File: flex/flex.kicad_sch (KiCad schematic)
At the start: 2 parts, among them J1 Conn_01x18_Pin

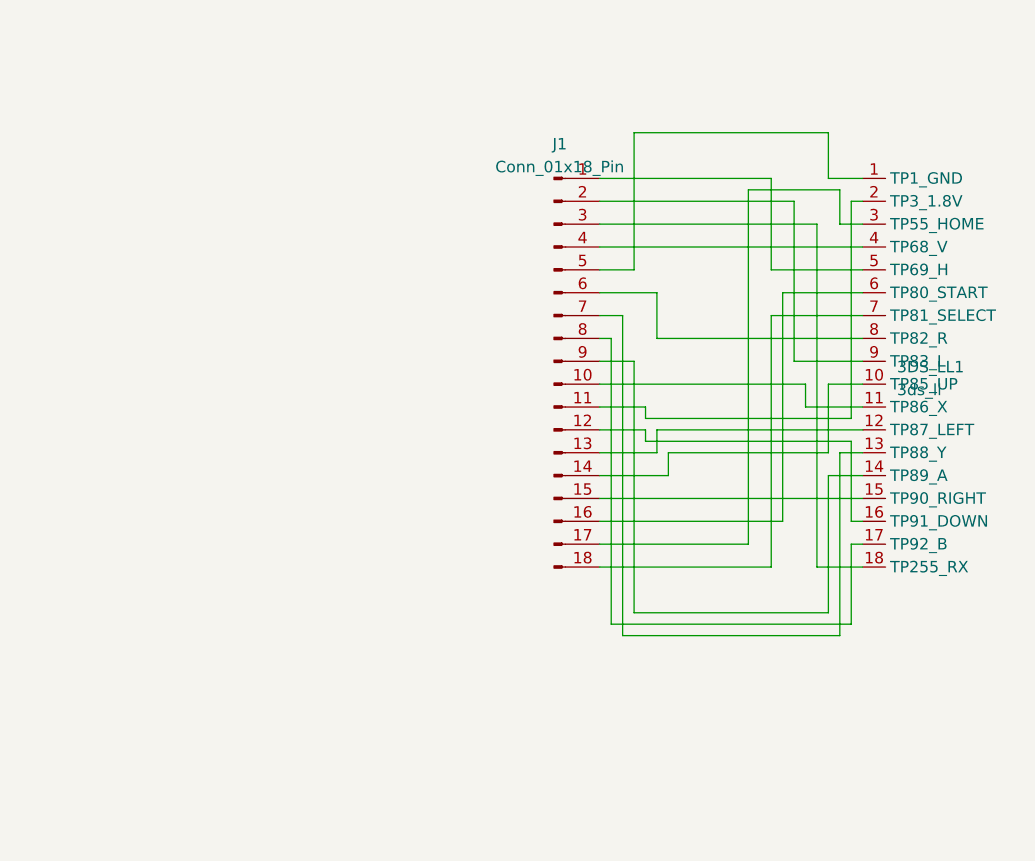
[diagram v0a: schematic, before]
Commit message: Extend flex to touch screen
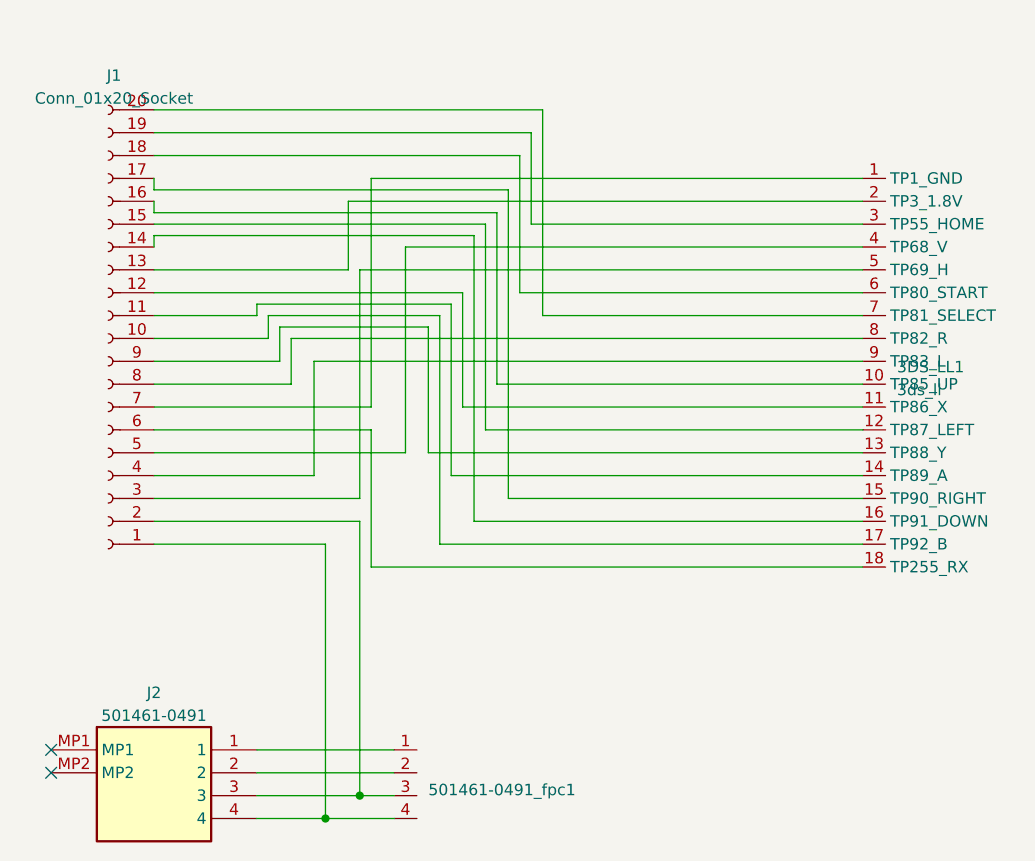
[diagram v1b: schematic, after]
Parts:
- removed J1: Conn_01x18_Pin, Connector_PinHeader_2.54mm:PinHeader_1x18_P2.54mm_Vertical, symbol Connector:Conn_01x18_Pin
- added 501461-0491_fpc1: ~, 501461-0491_fpc:501461-0491_fpc, symbol 501461-0491_fpc:501461-0491_fpc
- added J1: Conn_01x20_Socket, Connector_PinHeader_2.54mm:PinHeader_1x20_P2.54mm_Vertical, symbol Connector:Conn_01x20_Socket
- added J2: 501461-0491, 501461-0491:5014610491, symbol 501461-0491:501461-0491
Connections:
- net at 3DS_LL1.5 (TP69_H): now also J1.3 (Pin_3)
- net at 3DS_LL1.11 (TP86_X): now also J1.12 (Pin_12)
- net at 3DS_LL1.2 (TP3_1.8V): now also J1.13 (Pin_13)
- net at 3DS_LL1.16 (TP91_DOWN): now also J1.14 (Pin_14)
- net at 3DS_LL1.12 (TP87_LEFT): now also J1.15 (Pin_15)
- net at 3DS_LL1.10 (TP85_UP): now also J1.16 (Pin_16)
- net at 3DS_LL1.15 (TP90_RIGHT): now also J1.17 (Pin_17)
- net at 3DS_LL1.6 (TP80_START): now also J1.18 (Pin_18)
- net at 3DS_LL1.3 (TP55_HOME): now also J1.19 (Pin_19)
- net at 3DS_LL1.7 (TP81_SELECT): now also J1.20 (Pin_20)
- net at 3DS_LL1.9 (TP83_L): now also J1.4 (Pin_4)
- net at 3DS_LL1.18 (TP255_RX): now also J1.6 (Pin_6)
- net at 3DS_LL1.4 (TP68_V): now also J1.5 (Pin_5)
- net at 3DS_LL1.1 (TP1_GND): now also J1.7 (Pin_7)
- net at 3DS_LL1.8 (TP82_R): now also J1.8 (Pin_8)
- net at 3DS_LL1.13 (TP88_Y): now also J1.9 (Pin_9)
- net at 3DS_LL1.17 (TP92_B): now also J1.10 (Pin_10)
- net at 3DS_LL1.14 (TP89_A): now also J1.11 (Pin_11)
- new net: 501461-0491_fpc1.4, J1.1 (Pin_1), J2.4
- new net: 501461-0491_fpc1.3, J1.2 (Pin_2), J2.3
- new net: 501461-0491_fpc1.1, J2.1
- new net: 501461-0491_fpc1.2, J2.2
- no-connect marks 0 -> 2

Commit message: Add fpc
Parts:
- removed 3DS_LL1: 3ds_ll, 3ds:3ds_ll, symbol 3ds:3ds_ll
- removed 501461-0491_fpc1: ~, 501461-0491_fpc:501461-0491_fpc, symbol 501461-0491_fpc:501461-0491_fpc
- removed J1: Conn_01x20_Socket, Connector_PinHeader_2.54mm:PinHeader_1x20_P2.54mm_Vertical, symbol Connector:Conn_01x20_Socket
- removed J2: 501461-0491, 501461-0491:5014610491, symbol 501461-0491:501461-0491
- added J1: Conn_01x24_Pin, lib:3ds_ll, symbol Connector:Conn_01x24_Pin
- added J2: Conn_01x24_Pin, lib:bss, symbol Connector:Conn_01x24_Pin
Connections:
- new net: J1.1 (Pin_1), J2.1 (Pin_1)
- new net: J1.10 (Pin_10), J2.10 (Pin_10)
- new net: J1.11 (Pin_11), J2.11 (Pin_11)
- new net: J1.12 (Pin_12), J2.12 (Pin_12)
- new net: J1.13 (Pin_13), J2.13 (Pin_13)
- new net: J1.14 (Pin_14), J2.14 (Pin_14)
- new net: J1.15 (Pin_15), J2.15 (Pin_15)
- new net: J1.16 (Pin_16), J2.16 (Pin_16)
- new net: J1.17 (Pin_17), J2.17 (Pin_17)
- new net: J1.18 (Pin_18), J2.18 (Pin_18)
- new net: J1.19 (Pin_19), J2.19 (Pin_19)
- new net: J1.2 (Pin_2), J2.2 (Pin_2)
- new net: J1.20 (Pin_20), J2.20 (Pin_20)
- new net: J1.21 (Pin_21), J2.21 (Pin_21)
- new net: J1.22 (Pin_22), J2.22 (Pin_22)
- new net: J1.23 (Pin_23), J2.23 (Pin_23)
- new net: J1.24 (Pin_24), J2.24 (Pin_24)
- new net: J1.3 (Pin_3), J2.3 (Pin_3)
- new net: J1.4 (Pin_4), J2.4 (Pin_4)
- new net: J1.5 (Pin_5), J2.5 (Pin_5)
- new net: J1.6 (Pin_6), J2.6 (Pin_6)
- new net: J1.7 (Pin_7), J2.7 (Pin_7)
- new net: J1.8 (Pin_8), J2.8 (Pin_8)
- new net: J1.9 (Pin_9), J2.9 (Pin_9)
- no-connect marks 2 -> 0

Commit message: flex
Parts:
- J2: footprint lib:bss -> THD0515-24CL-SN_FPC:THD0515-24CL-SN_FPC
- e1: renamed from J1; footprint lib:3ds_ll -> 3DS_LL:3DS_LL
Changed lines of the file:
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@@
   (symbol (lib_id "Connector:Conn_01x24_Pin") (at 71.12 78.74 0) (unit 1)
     (in_bom yes) (on_board yes) (dnp no) (fields_autoplaced)
-    (property "Reference" "J1" (at 71.755 46.99 0)
+    (property "Reference" "e1" (at 71.755 46.99 0)
       (effects (font (size 1.27 1.27)))
     )
@@
       (effects (font (size 1.27 1.27)))
     )
-    (property "Footprint" "lib:3ds_ll" (at 71.12 78.74 0)
+    (property "Footprint" "3DS_LL:3DS_LL" (at 71.12 78.74 0)
       (effects (font (size 1.27 1.27)) hide)
     )
@@
       (project "flex"
         (path "/9ae2b03a-48a0-445d-83ec-edfc9c6f4ccc"
-          (reference "J1") (unit 1)
+          (reference "e1") (unit 1)
         )
       )
@@
       (effects (font (size 1.27 1.27)))
     )
-    (property "Footprint" "lib:bss" (at 93.98 78.74 0)
+    (property "Footprint" "THD0515-24CL-SN_FPC:THD0515-24CL-SN_FPC" (at 93.98 78.74 0)
       (effects (font (size 1.27 1.27)) hide)
     )
